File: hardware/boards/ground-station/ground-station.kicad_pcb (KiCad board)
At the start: 2 copper layers, 65 x 56.5 mm, 5 parts, among them J101 Raspberry_Pi_2_3

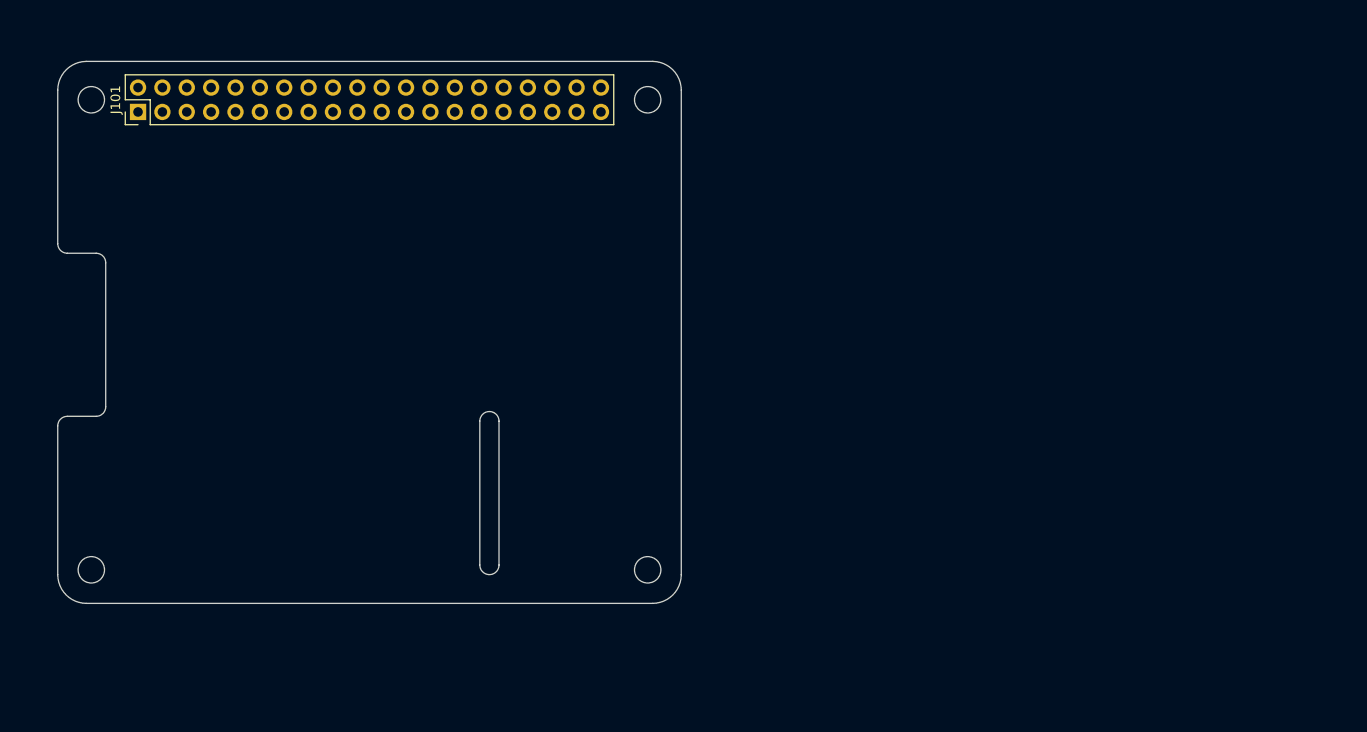
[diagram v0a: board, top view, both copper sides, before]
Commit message: Did initial layout. Still need to connect everything together
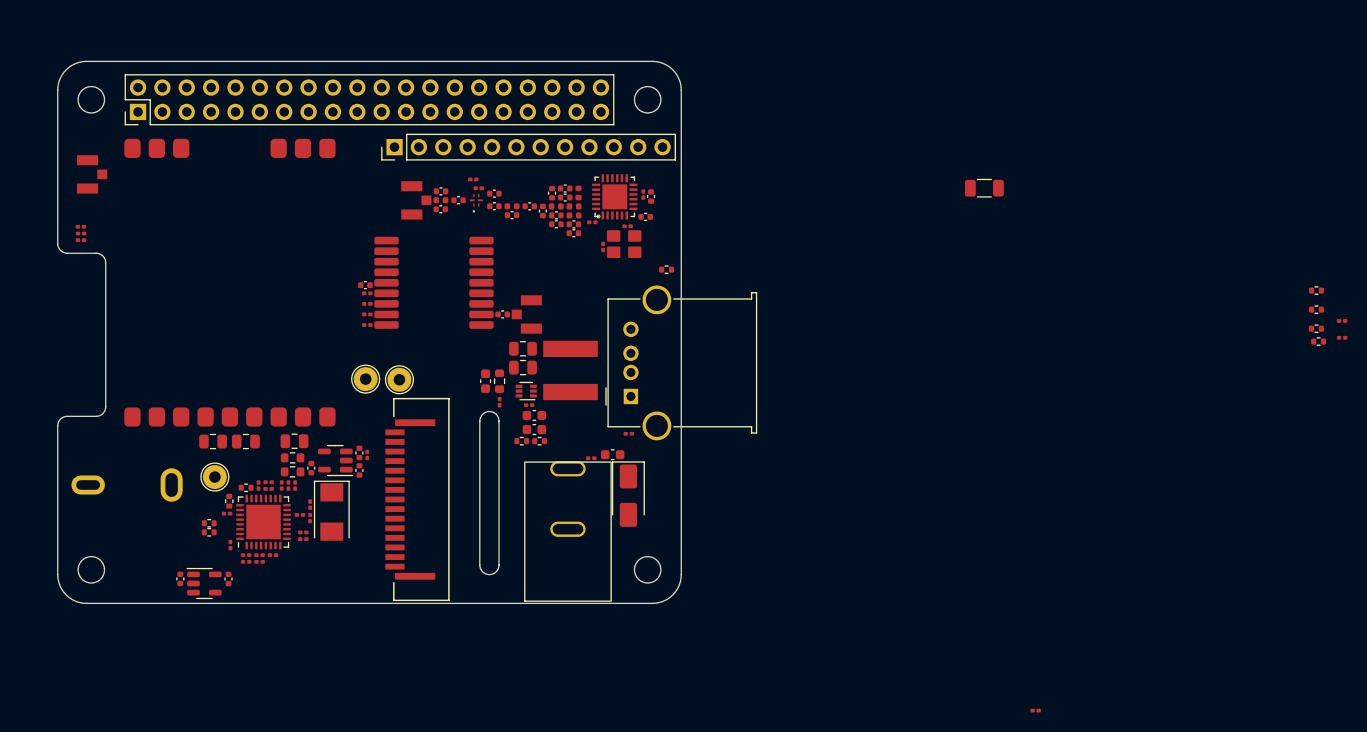
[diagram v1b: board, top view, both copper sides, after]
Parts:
- added C1: 100n, Capacitor_SMD:C_0201_0603Metric, F.Cu at (159.7, 104.7)
- added C2: ~, Capacitor_SMD:C_0603_1608Metric, F.Cu at (144.8, 99.2)
- added C201: 22u, Capacitor_SMD:C_0805_2012Metric, F.Cu at (119.8, 105.5)
- added C202: 22u, Capacitor_SMD:C_0805_2012Metric, F.Cu at (116.4, 105.5)
- added C203: 22u, Capacitor_SMD:C_0805_2012Metric, F.Cu at (124.9, 105.5)
- added C204: 470n, Capacitor_SMD:C_0402_1005Metric, F.Cu at (161.5, 82.1)
- added C205: 100n, Capacitor_SMD:C_0201_0603Metric, F.Cu at (132.5, 92.3)
- added C206: 100n, Capacitor_SMD:C_0201_0603Metric, F.Cu at (132.5, 91.2)
- added C207: 100n, Capacitor_SMD:C_0201_0603Metric, F.Cu at (132.5, 90.1)
- added C208: 2.2u, Capacitor_SMD:C_0402_1005Metric, F.Cu at (132.3, 89.2)
- added C209: 47p, Capacitor_SMD:C_0402_1005Metric, F.Cu at (146.6, 92.3)
- added C210: 100n, Capacitor_SMD:C_0201_0603Metric, F.Cu at (161.2, 79.8)
- added C211: 1u, Capacitor_SMD:C_0402_1005Metric, F.Cu at (162.0, 80.0)
- added C212: 16p, Capacitor_SMD:C_0201_0603Metric, F.Cu at (157.0, 85.2)
- added C213: 47n, Capacitor_SMD:C_0402_1005Metric, F.Cu at (154.0, 83.8)
- added C214: 16p, Capacitor_SMD:C_0201_0603Metric, F.Cu at (159.6, 83.1)
- added C215: 47p, Capacitor_SMD:C_0402_1005Metric, F.Cu at (154.0, 82.9)
- added C216: 1.8p, Capacitor_SMD:C_0402_1005Metric, F.Cu at (153.1, 79.1)
- added C217: 2.4p, Capacitor_SMD:C_0402_1005Metric, F.Cu at (153.1, 80.1)
- added C218: 1n, Capacitor_SMD:C_0402_1005Metric, F.Cu at (151.7, 79.6)
- added C219: 5.6p, Capacitor_SMD:C_0402_1005Metric, F.Cu at (152.2, 82.9)
- added C220: 3p, Capacitor_SMD:C_0402_1005Metric, F.Cu at (152.2, 81.9)
- added C221: 5.6p, Capacitor_SMD:C_0402_1005Metric, F.Cu at (150.8, 81.5)
- added C222: 39p, Capacitor_SMD:C_0402_1005Metric, F.Cu at (149.4, 81.0)
- added C223: 1.8p, Capacitor_SMD:C_0402_1005Metric, F.Cu at (147.6, 81.9)
- added C224: 1n, Capacitor_SMD:C_0402_1005Metric, F.Cu at (145.7, 81.0)
- added C225: 1n, Capacitor_SMD:C_0402_1005Metric, F.Cu at (145.7, 79.7)
- added C226: 1n, Capacitor_SMD:C_0201_0603Metric, F.Cu at (144.1, 79.1)
- added C227: 10n, Capacitor_SMD:C_0201_0603Metric, F.Cu at (155.9, 82.7)
- added C228: 39p, Capacitor_SMD:C_0402_1005Metric, F.Cu at (142.0, 80.4)
- added C229: 3.3p, Capacitor_SMD:C_0402_1005Metric, F.Cu at (140.1, 79.4)
- added C23: 10u, Capacitor_SMD:C_0603_1608Metric, F.Cu at (158.0, 106.9)
- added C230: 3.3p, Capacitor_SMD:C_0402_1005Metric, F.Cu at (140.1, 81.3)
- added C24: 100n, Capacitor_SMD:C_0201_0603Metric, F.Cu at (155.8, 107.2)
- added C25: 10u, Capacitor_SMD:C_0603_1608Metric, F.Cu at (149.9, 102.8)
- added C26: 10u, Capacitor_SMD:C_0603_1608Metric, F.Cu at (149.9, 104.3)
- added C27: 100n, Capacitor_SMD:C_0201_0603Metric, F.Cu at (149.3, 101.7)
- added C3: 100n, Capacitor_SMD:C_0201_0603Metric, F.Cu at (123.5, 110.1)
- added C33: 22u, Capacitor_SMD:C_0805_2012Metric, F.Cu at (148.7, 97.8)
- added C34: 22u, Capacitor_SMD:C_0805_2012Metric, F.Cu at (148.7, 95.8)
- added C602: 22p, Capacitor_SMD:C_0201_0603Metric, F.Cu at (126.5, 112.1)
- added C603: 22p, Capacitor_SMD:C_0201_0603Metric, F.Cu at (126.5, 113.5)
- added C604: 100n, Capacitor_SMD:C_0201_0603Metric, F.Cu at (122.2, 110.5)
- added C605: 1u, Capacitor_SMD:C_0402_1005Metric, F.Cu at (131.6, 108.5)
- added C606: 1u, Capacitor_SMD:C_0402_1005Metric, F.Cu at (113.0, 119.8)
- added C607: 1u, Capacitor_SMD:C_0402_1005Metric, F.Cu at (126.6, 108.3)
- added C608: 1u, Capacitor_SMD:C_0402_1005Metric, F.Cu at (118.0, 119.8)
- added C610: 680n, Capacitor_SMD:C_0402_1005Metric, F.Cu at (131.6, 106.7)
- added C611: 100n, Capacitor_SMD:C_0201_0603Metric, F.Cu at (119.8, 118.0)
- added C612: 10n, Capacitor_SMD:C_0201_0603Metric, F.Cu at (119.8, 117.3)
- added C613: 10n, Capacitor_SMD:C_0201_0603Metric, F.Cu at (121.2, 117.3)
- added C614: 100n, Capacitor_SMD:C_0201_0603Metric, F.Cu at (121.2, 118.0)
- added C615: 100n, Capacitor_SMD:C_0201_0603Metric, F.Cu at (125.8, 115.7)
- added C616: 10n, Capacitor_SMD:C_0201_0603Metric, F.Cu at (125.8, 115.0)
- added C617: 10n, Capacitor_SMD:C_0201_0603Metric, F.Cu at (124.2, 110.1)
- added C618: 100n, Capacitor_SMD:C_0201_0603Metric, F.Cu at (124.9, 110.1)
- added C619: 10n, Capacitor_SMD:C_0201_0603Metric, F.Cu at (121.1, 110.1)
- added C620: 100n, Capacitor_SMD:C_0201_0603Metric, F.Cu at (122.2, 109.8)
- added D401: SMAJ5.0A, Diode_SMD:D_SMA, F.Cu at (159.7, 111.2)
- added J1: USB_A, Connector_USB:USB_A_Molex_67643_Horizontal, F.Cu at (159.9, 100.8)
- added J102: Conn_01x15, capstone:CON15_1X15_DRB_SFW, F.Cu at (132.6, 111.5)
- added J2: Barrel_Jack, capstone:PJ-037A, F.Cu at (153.4, 114.7)
- added J201: U.FL, capstone:U.FL-R-SMT-1(60), F.Cu at (103.3, 77.7)
- added J202: U.FL, capstone:U.FL-R-SMT-1(60), F.Cu at (149.6, 92.3)
- added J203: U.FL, capstone:U.FL-R-SMT-1(60), F.Cu at (137.1, 80.4)
- added J3: Conn_Coaxial, capstone:RCJ-054, F.Cu at (106.7, 110.0)
- added J5: Conn_01x12, Connector_PinHeader_2.54mm:PinHeader_1x12_P2.54mm_Vertical, F.Cu at (135.3, 74.8)
- added L201: 0R, Inductor_SMD:L_0402_1005Metric, F.Cu at (154.0, 81.0)
- added L202: 47n, Inductor_SMD:L_0402_1005Metric, F.Cu at (154.0, 81.9)
- added L203: 15n, Inductor_SMD:L_0402_1005Metric, F.Cu at (154.5, 79.6)
- added L204: 2.5n, Inductor_SMD:L_0402_1005Metric, F.Cu at (152.2, 81.0)
- added L205: 4.7n, Inductor_SMD:L_0402_1005Metric, F.Cu at (147.6, 81.0)
- added L206: 9.1n, Inductor_SMD:L_0402_1005Metric, F.Cu at (140.1, 80.4)
- added L4: 1.5u, capstone:FNR6028S1R5MT, F.Cu at (153.6, 98.1)
- added R1: 0, Resistor_SMD:R_0402_1005Metric, F.Cu at (163.7, 87.6)
- added R101: 4.7k, Resistor_SMD:R_0201_0603Metric, F.Cu at (234.1, 92.9)
- added R102: 4.7k, Resistor_SMD:R_0201_0603Metric, F.Cu at (234.1, 94.7)
- added R2: 0, Resistor_SMD:R_0402_1005Metric, F.Cu at (150.4, 105.5)
- added R201: 100k, Resistor_SMD:R_0201_0603Metric, F.Cu at (202.1, 133.6)
- added R202: 10k, Resistor_SMD:R_0201_0603Metric, F.Cu at (102.6, 84.5)
- added R203: 10k, Resistor_SMD:R_0201_0603Metric, F.Cu at (102.6, 83.8)
- added R204: 10k, Resistor_SMD:R_0201_0603Metric, F.Cu at (102.6, 83.1)
- added R205: 100k, Resistor_SMD:R_0201_0603Metric, F.Cu at (132.5, 93.4)
- added R206: 100R, Resistor_SMD:R_0201_0603Metric, F.Cu at (143.5, 78.2)
- added R22: 0, Resistor_SMD:R_0402_1005Metric, F.Cu at (118.1, 111.7)
- added R23: 0, Resistor_SMD:R_0402_1005Metric, F.Cu at (231.4, 89.8)
- added R24: 0, Resistor_SMD:R_0402_1005Metric, F.Cu at (231.4, 91.8)
- added R25: 0, Resistor_SMD:R_0402_1005Metric, F.Cu at (231.4, 93.8)
- added R26: 0, Resistor_SMD:R_0402_1005Metric, F.Cu at (231.6, 95.1)
- added R27: 0, Resistor_SMD:R_0402_1005Metric, F.Cu at (116.0, 115.0)
- added R28: 0, Resistor_SMD:R_0402_1005Metric, F.Cu at (116.0, 114.0)
- added R3: 0, Resistor_SMD:R_1206_3216Metric, F.Cu at (196.8, 79.1)
- added R301: 47R, Resistor_SMD:R_0201_0603Metric, F.Cu at (122.6, 117.3)
- added R4: 24R, Resistor_SMD:R_0603_1608Metric, F.Cu at (124.7, 107.2)
- added R5: 51R, Resistor_SMD:R_0603_1608Metric, F.Cu at (124.7, 108.7)
- added R6: 0, Resistor_SMD:R_0402_1005Metric, F.Cu at (119.8, 110.3)
- added R603: 1k, Resistor_SMD:R_0201_0603Metric, F.Cu at (125.4, 113.2)
- added R604: 100k, Resistor_SMD:R_0201_0603Metric, F.Cu at (118.2, 116.3)
- added R605: 100k, Resistor_SMD:R_0201_0603Metric, F.Cu at (117.8, 113.0)
- added R606: 10k, Resistor_SMD:R_0201_0603Metric, F.Cu at (132.4, 106.9)
- added R7: 100k, Resistor_SMD:R_0402_1005Metric, F.Cu at (148.6, 105.5)
- added R8: 135k, Resistor_SMD:R_0603_1608Metric, F.Cu at (146.2, 99.2)
- added R9: 30k, Resistor_SMD:R_0201_0603Metric, F.Cu at (146.2, 101.4)
- added TP1: TestPoint, TestPoint:TestPoint_THTPad_D2.5mm_Drill1.2mm, F.Cu at (135.8, 99.1)
- added TP2: TestPoint, TestPoint:TestPoint_THTPad_D2.5mm_Drill1.2mm, F.Cu at (132.3, 99.0)
- added TP3: TestPoint, TestPoint:TestPoint_THTPad_D2.5mm_Drill1.2mm, F.Cu at (116.6, 109.2)
- added U201: SX1262IMLTRT, capstone:SX1262IMLTRT, F.Cu at (158.3, 80.0)
- added U202: RX5808, capstone:RX5808, F.Cu at (117.9, 89.0)
- added U203: SW-GPS01, capstone:SW-GPS01, F.Cu at (139.1, 85.0)
- added U204: SKY13453-385LF, capstone:IC_SKY13453-385LF, F.Cu at (143.8, 80.4)
- added U3: TPS564242DRLR, Package_TO_SOT_SMD:SOT-563, F.Cu at (149.0, 100.2)
- added U601: ADV7282A-M, Package_DFN_QFN:QFN-32-1EP_5x5mm_P0.5mm_EP3.6x3.6mm, F.Cu at (121.6, 113.9)
- added U602: AP2127K-1.8, Package_TO_SOT_SMD:SOT-23-5, F.Cu at (115.5, 120.3)
- added U603: AP2127K-1.8, Package_TO_SOT_SMD:SOT-23-5, F.Cu at (129.1, 107.5)
- added Y201: 32 MHz, capstone:JYJE-3TJ432000HYFBC, F.Cu at (157.5, 84.9)
- added Y601: 28.63636 MHz, Crystal:Crystal_SMD_Abracon_ABM3-2Pin_5.0x3.2mm, F.Cu at (128.8, 112.8)
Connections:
- J101 pad 10: unconnected-(J101-GPIO15/RXD-Pad10) -> /GPS_UART_TX
- J101 pad 13: unconnected-(J101-GPIO27-Pad13) -> /VIDEO_CH3
- J101 pad 14: unconnected-(J101-GND-Pad14) -> GND
- J101 pad 15: unconnected-(J101-GPIO22-Pad15) -> /~{DIGITIZER_PWRDWN}
- J101 pad 16: unconnected-(J101-GPIO23-Pad16) -> /~{DIGITIZER_RESET}
- J101 pad 19: unconnected-(J101-MOSI0/GPIO10-Pad19) -> /DIGITAL_RADIO_MOSI
- J101 pad 2: unconnected-(J101-5V-Pad2) -> Net-(J101-5V-Pad2)
- J101 pad 20: unconnected-(J101-GND-Pad20) -> GND
- J101 pad 21: unconnected-(J101-MISO0/GPIO9-Pad21) -> /DIGITAL_RADIO_MISO
- J101 pad 22: unconnected-(J101-GPIO25-Pad22) -> /VIDEO_CH1
- J101 pad 23: unconnected-(J101-SCLK0/GPIO11-Pad23) -> /DIGITAL_RADIO_SCLK
- J101 pad 24: unconnected-(J101-~{CE0}/GPIO8-Pad24) -> /~{DIGITAL_RADIO_nCS}
- J101 pad 25: unconnected-(J101-GND-Pad25) -> GND
- J101 pad 26: unconnected-(J101-~{CE1}/GPIO7-Pad26) -> /~{DIGITAL_RADIO_RESET}
- J101 pad 29: unconnected-(J101-GCLK1/GPIO5-Pad29) -> /DIGITAL_RADIO_DIO3
- J101 pad 3: unconnected-(J101-SDA/GPIO2-Pad3) -> /I2C_SDA
- J101 pad 30: unconnected-(J101-GND-Pad30) -> GND
- J101 pad 31: unconnected-(J101-GCLK2/GPIO6-Pad31) -> /DIGITAL_RADIO_BUSY
- J101 pad 33: unconnected-(J101-PWM1/GPIO13-Pad33) -> /~{DIGITIZER_INTRQ}
- J101 pad 34: unconnected-(J101-GND-Pad34) -> GND
- J101 pad 36: unconnected-(J101-GPIO16-Pad36) -> /~{GPS_RESET}
- J101 pad 37: unconnected-(J101-GPIO26-Pad37) -> /VIDEO_CH2
- J101 pad 39: unconnected-(J101-GND-Pad39) -> GND
- J101 pad 4: unconnected-(J101-5V-Pad4) -> Net-(J101-5V-Pad2)
- J101 pad 5: unconnected-(J101-SCL/GPIO3-Pad5) -> /I2C_SCL
- J101 pad 6: unconnected-(J101-GND-Pad6) -> GND
- J101 pad 7: unconnected-(J101-GCLK0/GPIO4-Pad7) -> /DIGITAL_RADIO_DIO1
- J101 pad 8: unconnected-(J101-GPIO14/TXD-Pad8) -> /GPS_UART_RX
- J101 pad 9: unconnected-(J101-GND-Pad9) -> GND
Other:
- copper layers 2 -> 4

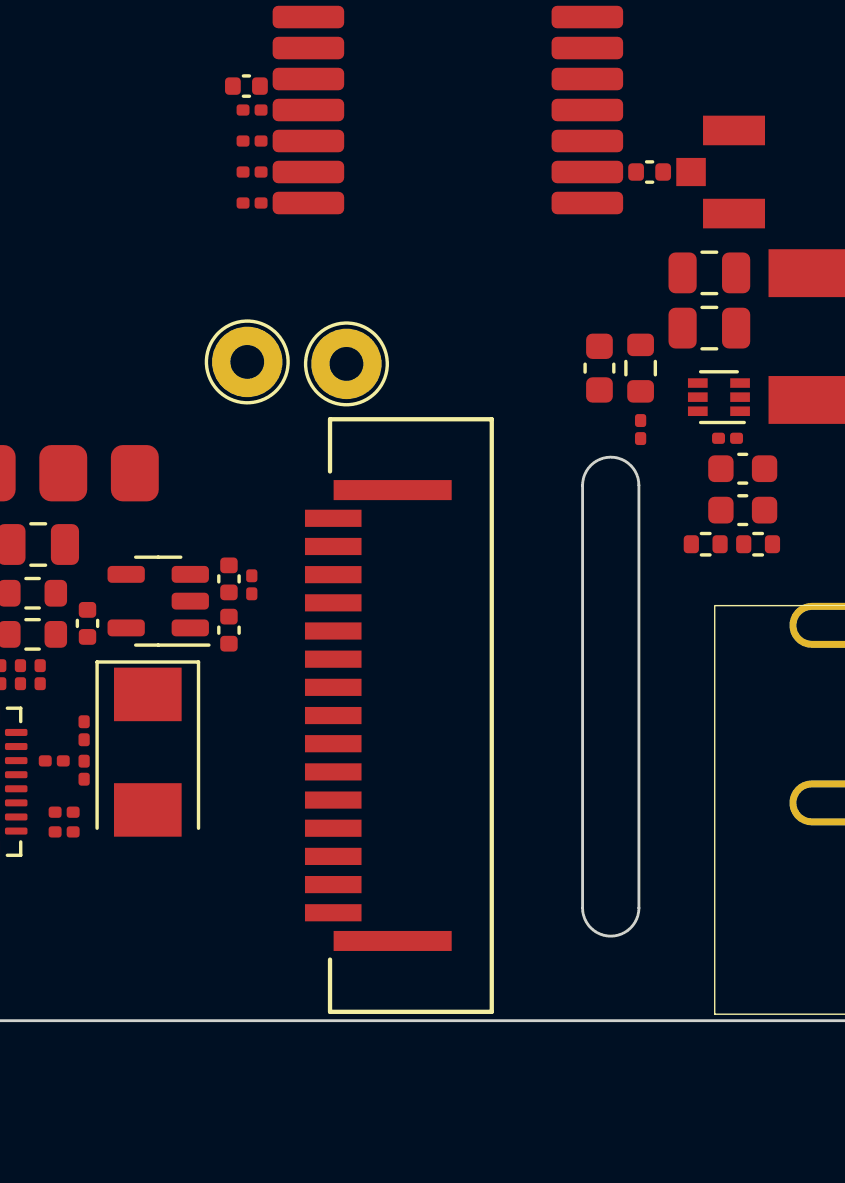
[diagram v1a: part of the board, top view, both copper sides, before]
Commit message: Removed 10 pin radio header and changed ribbon cable connector
- disconnected 3V3 from the ribbon cable connector to keep the Pi 3V3 rail separate from the board 3V3 rail
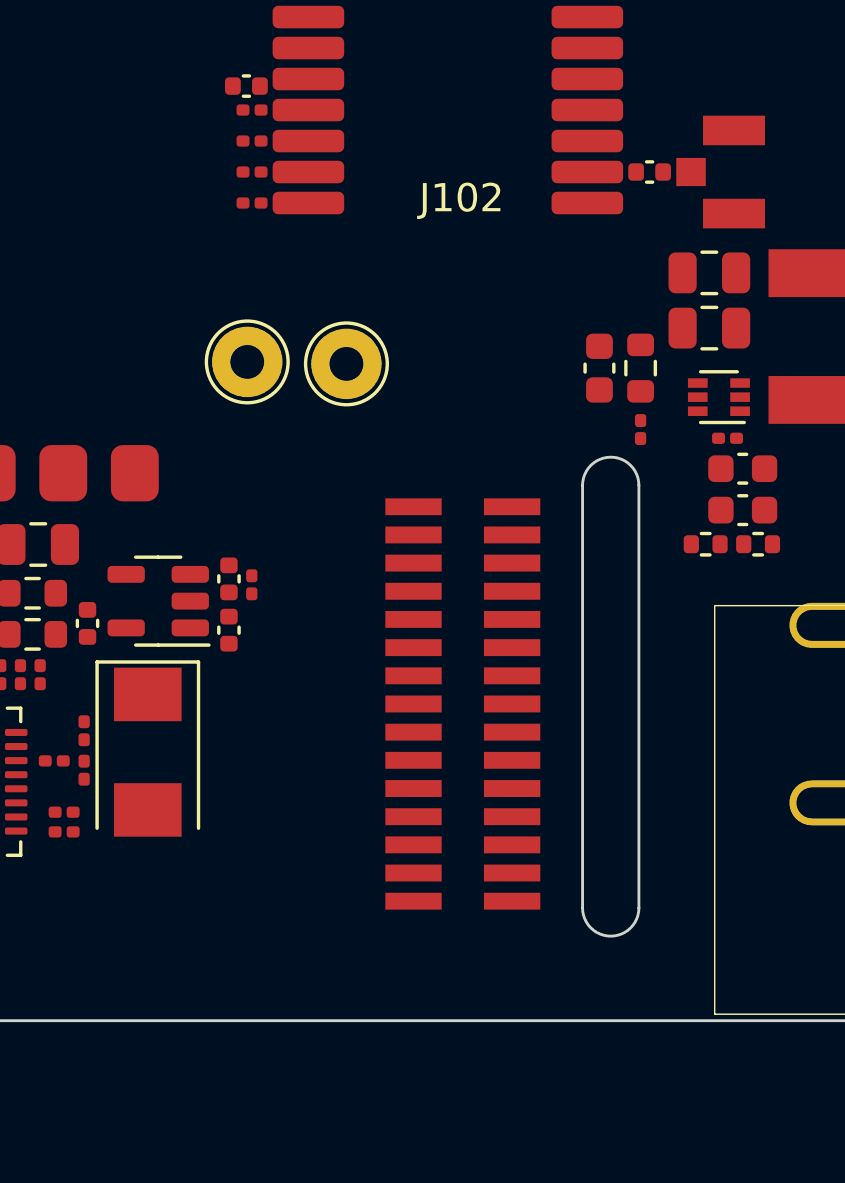
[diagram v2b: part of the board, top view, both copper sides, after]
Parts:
- J102: footprint capstone:CON15_1X15_DRB_SFW -> capstone:FFC3A20-15-G
- moved J102 7.37 mm to (139.9, 111.1), turned to 0 degrees
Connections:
- J102 pad 15: +3V3 -> unconnected-(J102-Pin_15-Pad15)

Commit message: layout
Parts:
- removed J5: Conn_01x12, Connector_PinHeader_2.54mm:PinHeader_1x12_P2.54mm_Vertical
- removed R101, R102: 4.7k, Resistor_SMD:R_0201_0603Metric
- moved R23 92.6 mm to (140.6, 108.0), turned to 180 degrees
- moved R24 92.4 mm to (140.6, 109.0), turned to 180 degrees
- moved R26 91.6 mm to (140.7, 106.0), turned to 180 degrees
- moved R25 91.4 mm to (140.7, 105.0), turned to 180 degrees
- moved R201 72.0 mm to (158.5, 76.2), turned to 90 degrees
- moved R202 36.1 mm to (137.3, 74.7), turned to 90 degrees
- moved R203 35.2 mm to (136.6, 74.7), turned to 90 degrees
- moved R204 34.4 mm to (135.9, 74.7), turned to 90 degrees
- moved C214 3.66 mm to (156.2, 84.5), turned to -135 degrees
- moved C212 3.45 mm to (160.5, 85.0), turned to -45 degrees
- moved C615 3.34 mm to (129.0, 116.7)
- moved J102 3.04 mm to (136.9, 111.0)
- moved TP1 2.99 mm to (135.2, 96.2)
- moved Y201 2.77 mm to (159.6, 86.7), turned to -45 degrees
- moved C616 2.48 mm to (128.3, 115.1), turned to 90 degrees
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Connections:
- J101 pad 3: /I2C_SDA -> unconnected-(J101-SDA/GPIO2-Pad3)
- J101 pad 5: /I2C_SCL -> unconnected-(J101-SCL/GPIO3-Pad5)
- R23 pad 1: /CAM_D1_N -> /CAM_D0_N
- R24 pad 1: /CAM_D1_P -> /CAM_D0_P
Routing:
- net /CAM_D0_N: track 0.00 -> 39.7 mm, vias 0 -> 4
- net /CAM_D0_P: track 0.00 -> 34.4 mm
- net /Video Digitizer/DIGITIZER_DIGITAL_SUPPLY: track 0.00 -> 23.7 mm, vias 0 -> 2
- net /CAM_CK_N: track 0.00 -> 23.1 mm
- net /CAM_CK_P: track 0.00 -> 22.8 mm
- net /Radios/VIDEO_OUT: track 0.00 -> 20.2 mm, vias 0 -> 1
- net /Radios/DIO2: track 0.00 -> 19.5 mm
- net Net-(J1-Shield): track 0.00 -> 15.8 mm
- net Net-(U601-AIN2): track 0.00 -> 9.73 mm
- net +3V3: track 0.00 -> 9.60 mm, vias 0 -> 5
- net Net-(U3-EN): track 0.00 -> 8.98 mm, vias 0 -> 2
- net /Video Digitizer/DIGITIZER_ANALOG_SUPPLY: track 0.00 -> 8.33 mm, vias 0 -> 2
- net Net-(U601-XTALN): track 0.00 -> 7.32 mm
- net Net-(J201-In): track 0.00 -> 6.82 mm
- net /Radios/SW_RX: track 0.00 -> 6.66 mm
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- added copper zone on F.Cu, net +3V3
- added copper zone on F.Cu, net +5V
- added copper zone on F.Cu, net /Video Digitizer/DIGITIZER_ANALOG_SUPPLY
- added copper zone on F.Cu, net GND
- added copper zone on In1.Cu, net GND
- added copper zone on F.Cu, net Net-(U201-VREG)
- added copper zone on F.Cu, net Net-(U3-SW)
